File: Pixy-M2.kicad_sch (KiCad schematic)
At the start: 50 parts, among them J1 USB_C_Receptacle_USB2.0_14P, J2 Conn_01x22_Pin, J3 Conn_01x22_Pin, Q1 AO4407A, SW1 SW_Push, SW2 SW_Push, SW3 JS102011SAQN, U1 ESP32-S3-WROOM-1-N16, U2 USBLC6-2SC6, U3 AP63203WU

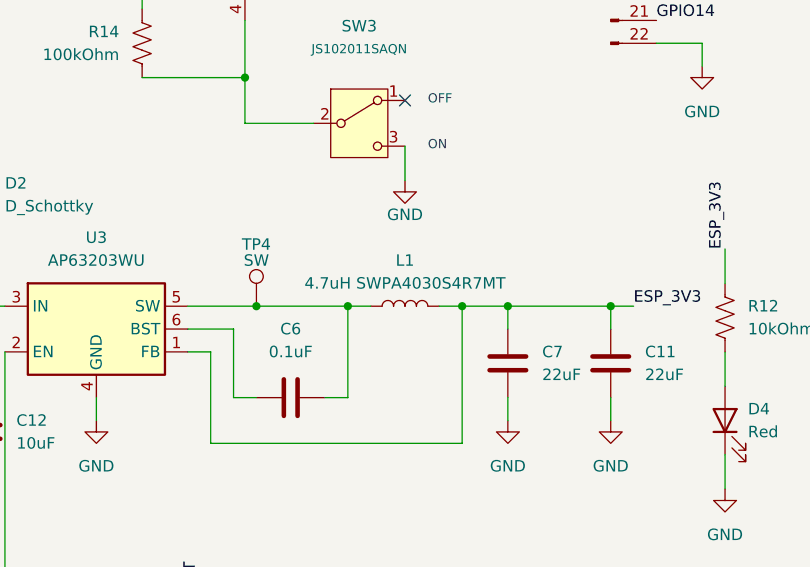
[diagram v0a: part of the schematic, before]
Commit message: Make L1 value and footprint name the same part (issue 1)
L1's Value named a Sunlord SWPA4030S4R7MT (4.0x4.0mm) while its Footprint
was the Bourns SRP5030T land pattern (5.0x5.0mm). The two are not
interchangeable -- Bourns is 2.0x1.8mm pads on a 4.5mm pitch, Sunlord
1.1x3.7mm pads on a 3.0mm pitch -- so the part would not have sat on its
pads. This was the last item blocking layout.

Settle on the Bourns SRP5030T-4R7M, keeping the footprint already
assigned, and write Value, MPN, Datasheet and Description together so the
component cannot go half-updated again. Ratings confirmed against the
datasheet: 4.7uH +/-20%, DCR 53mOhm max, Irms 4.6A, Isat 6A. Earlier notes
quoted the 4.6A Irms figure as the rated current; the saturation rating is
6A, against a ~700mA peak inductor current.

The Sunlord part works electrically and Inductor_SMD:L_Sunlord_SWPA4030S
exists in the stock library, so the decision is reversible -- but both
fields have to move together.

Netlist diff before/after shows only L1's own field text changing; no net,
pin or footprint assignment moved. ERC unchanged at 0 errors and the same
two GPIO45/GPIO46 isolated-label warnings. Sheet rendered and checked: the
new Value string sits clear of TP4, C6 and the SW wire.

Update the issue-1 section and status lines in CLAUDE.md, and the stale L1
row and ordering bullet in BOM.md.

Co-Authored-By: Claude Opus 5 <noreply@anthropic.com>
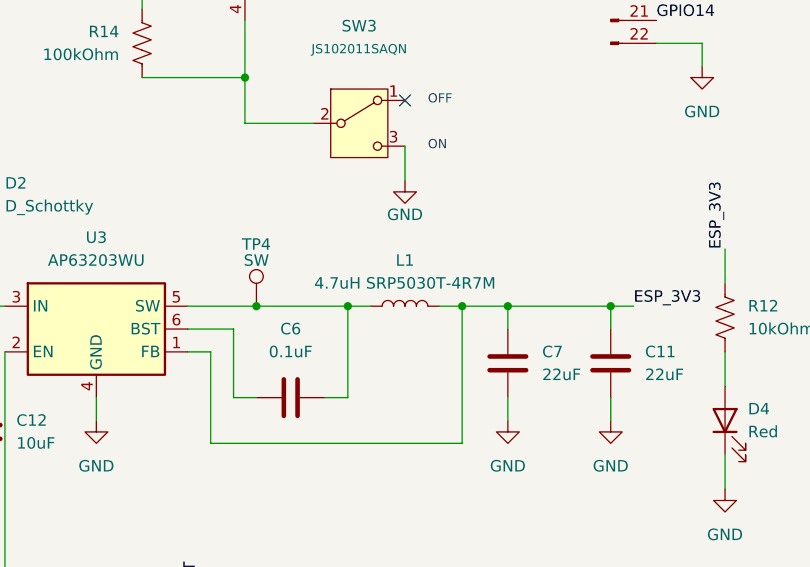
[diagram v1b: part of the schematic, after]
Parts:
- L1: value 4.7uH SWPA4030S4R7MT -> 4.7uH SRP5030T-4R7M; MPN (none) -> SRP5030T-4R7M
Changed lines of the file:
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@@
 			)
 		)
-		(property "Value" "4.7uH SWPA4030S4R7MT"
+		(property "Value" "4.7uH SRP5030T-4R7M"
 			(at 203.2 110.49 90)
 			(show_name no)
@@
 			)
 		)
-		(property "Datasheet" ""
+		(property "Datasheet" "https://www.bourns.com/docs/product-datasheets/srp5030t.pdf"
 			(at 203.2 113.03 0)
 			(hide yes)
@@
 			)
 		)
-		(property "Description" "Inductor"
+		(property "Description" "Buck inductor: Bourns SRP5030T-4R7M, 4.7uH +/-20%, DCR 53mOhm max, Irms 4.6A, Isat 6A, shielded, 5.0x5.0x3.0mm"
 			(at 203.2 113.03 0)
 			(hide yes)
+			(show_name no)
+			(do_not_autoplace no)
+			(effects
+				(font
+					(size 1.27 1.27)
+				)
+			)
+		)
+		(property "MPN" "SRP5030T-4R7M"
+			(at 203.2 113.03 0)
+			(hide yes)

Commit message: Add VL53L0X ToF sensor connectors (issue 14)
Wall sensing existed only as an architectural note -- CLAUDE.md said "IR
emitters/receivers" would live on the daughterboard, and nothing in the
schematic reflected any sensor at all. Replace that with four VL53L0X
time-of-flight modules on cables.

The sensors stay off-board so they can be aimed mechanically at the maze
walls; this PCB carries only their connectors, the shared bus pull-ups and
the local rail decoupling. Eight components added:

- J4-J7: JST SM06B-SRSS-TB, 6-position SH 1.0mm side-entry receptacles,
  one per sensor, with the two MP mounting pegs tied to GND.
- R15, R16: 2.2k I2C pull-ups on GPIO8 (SDA) and GPIO9 (SCL) to ESP_3V3.
- C15, C16: 10uF 16V and 100nF 16V on the sensor rail at the connectors.

J4-J7 reproduce the fitted module's header -- GY-VL53L0XV2, silkscreen
HW-842 -- in its own order, so each cable is a straight 1:1 loom with no
crossovers to get wrong:

  1 VCC   -> ESP_3V3
  2 GND   -> GND
  3 SCL   -> GPIO9
  4 SDA   -> GPIO8
  5 GPIO1 -> no-connect (sensor interrupt, unused)
  6 XSHUT -> GPIO4 / GPIO5 / GPIO6 / GPIO7, one per sensor

Every VL53L0X powers up at address 0x29 and the address is volatile, so
four on one bus is only possible with a per-sensor XSHUT. GPIO4-7 are
dedicated to that.

3.3V needs no 2.8V rail or level shifter on this board: the datasheet gives
AVDD 2.6/2.8/3.5V recommended with a 3.6V absolute maximum, and the module
regulates VCC (3.0-5.0V in) to 2.8V itself and level-shifts SCL/SDA to the
VCC rail. That is why R15/R16 pull up to ESP_3V3.

R15/R16 = 2.2k follows the datasheet's "typically fitted only once per bus,
near the host" and its 1.5-2k recommendation for AVDD 2.8V at 400kHz,
scaled to 3.3V. It sinks 1.5mA against a 4mA VOL spec and gives a ~190ns
rise at ~100pF of bus plus cable, inside fast mode's 300ns. If the modules
carry their own 10k pull-ups, four in parallel with this pair lands near
1.2k -- 2.8mA, still legal.

GPIO1 is deliberately unwired; th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
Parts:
- added C15: 10uF 16V, Capacitor_SMD:C_0805_2012Metric, symbol Device:C
- added C16: 0.1uF 16V, Capacitor_SMD:C_0603_1608Metric, symbol Device:C
- added J4, J5, J6, J7: SM06B-SRSS-TB, Connector_JST:JST_SH_SM06B-SRSS-TB_1x06-1MP_P1.00mm_Horizontal, symbol Connector_Generic_MountingPin:Conn_01x06_MountingPin
- added R15, R16: 2.2kOhm, Resistor_SMD:R_0805_2012Metric, symbol Device:R_US
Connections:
- net ESP_3V3: now also C15.1, C16.1, J4.1 (Pin_1), J5.1 (Pin_1), J6.1 (Pin_1), J7.1 (Pin_1), R15.1, R16.1
- net GND: now also C15.2, C16.2, J4.2 (Pin_2), J4.MP (MountPin), J5.2 (Pin_2), J5.MP (MountPin), J6.2 (Pin_2), J6.MP (MountPin), J7.2 (Pin_2), J7.MP (MountPin)
- net GPIO4: now also J4.6 (Pin_6)
- net GPIO5: now also J5.6 (Pin_6)
- net GPIO6: now also J6.6 (Pin_6)
- net GPIO7: now also J7.6 (Pin_6)
- net GPIO8: now also J4.4 (Pin_4), J5.4 (Pin_4), J6.4 (Pin_4), J7.4 (Pin_4), R15.2
- net GPIO9: now also J4.3 (Pin_3), J5.3 (Pin_3), J6.3 (Pin_3), J7.3 (Pin_3), R16.2
- no-connect marks 1 -> 5
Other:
- note added: "1 VCC, 2 GND, 3 SCL (GPIO9), 4 SDA (GPIO8), 5 GPIO1 = sensor interrupt, not used, 6 XSHUT."
- note added: "C15/C16: local reservoir for the four modules; ~19mA average each while ranging, 40mA VCSEL peak."
- note added: "Drive GPIO4-7 OPEN-DRAIN: low to shut a sensor down, float to let the module pull it up."
- note added: "Firmware must pull every XSHUT low first, then release one at a time and re-address it."
- note added: "INT"
- note added: "Module VIN 3.0-5.0V, regulates to 2.8V on board. Firmware must set 2V8 I/O (reg 0x89 bit 0)."
- note added: "R15/R16: I2C bus pull-ups, fitted once per bus at the host - VL53L0X datasheet Fig. 3."
- note added: "The module pulls XSHUT up to its own 2V8 rail, so all four wake enabled at address 0x29."
- note added: "VL53L0X ToF modules (GY-VL53L0XV2) on cables. J4-J7 match the module header 1:1:"
